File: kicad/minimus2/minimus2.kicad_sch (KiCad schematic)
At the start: 73 parts, among them J1 PROG_SER, J2 LM, J3 LM, Q1 SSM6N58NU_LF, Q2 SSM6N58NU_LF, Q3 DMN3051L, SW1 RESET, SW2 USER_A, SW3 USER_B, U1 LSM6DSRTR, U2 STM32U575CITx, U3 DRV8835, U4 AS5047D, U5 AS5047D, U6 BCR420UFD-7

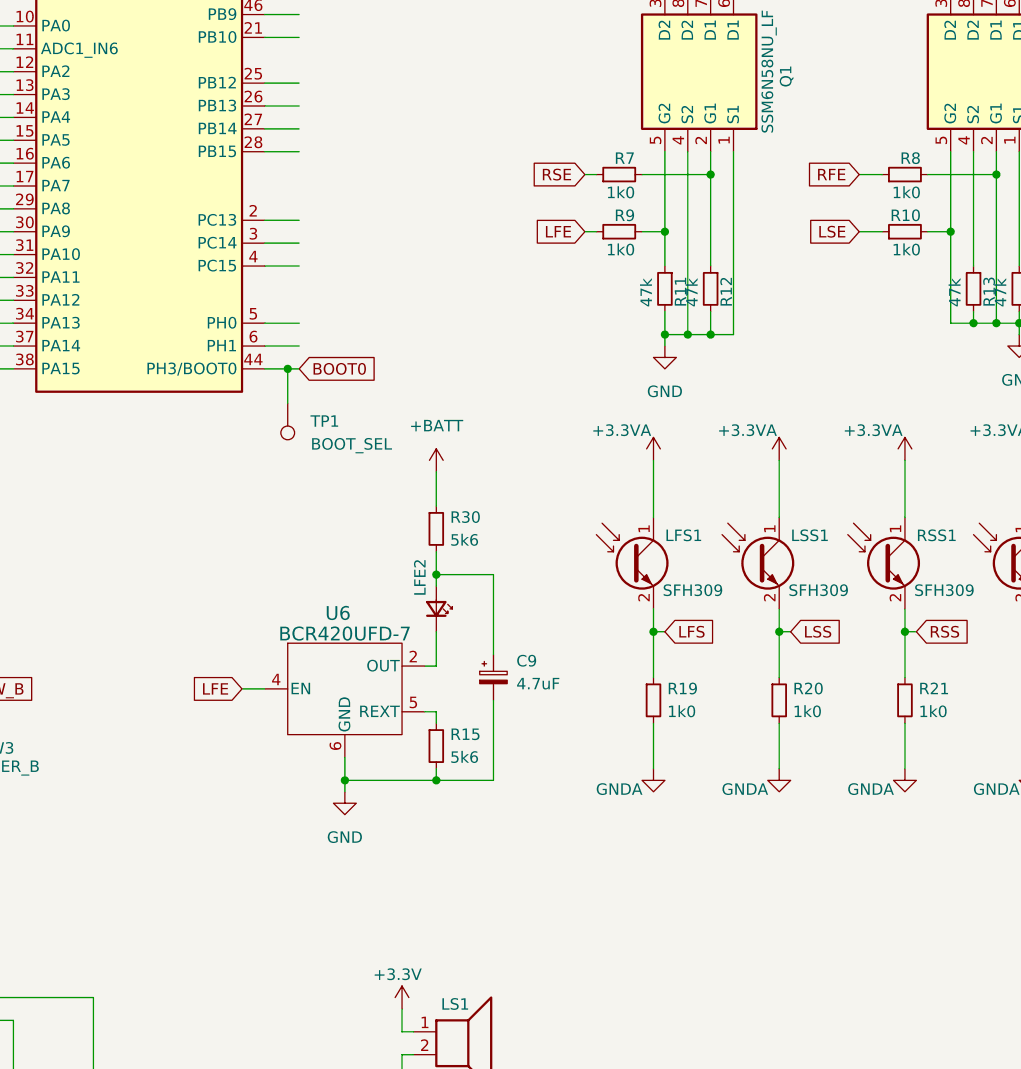
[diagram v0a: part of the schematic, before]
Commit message: rename the sensor emitter nets
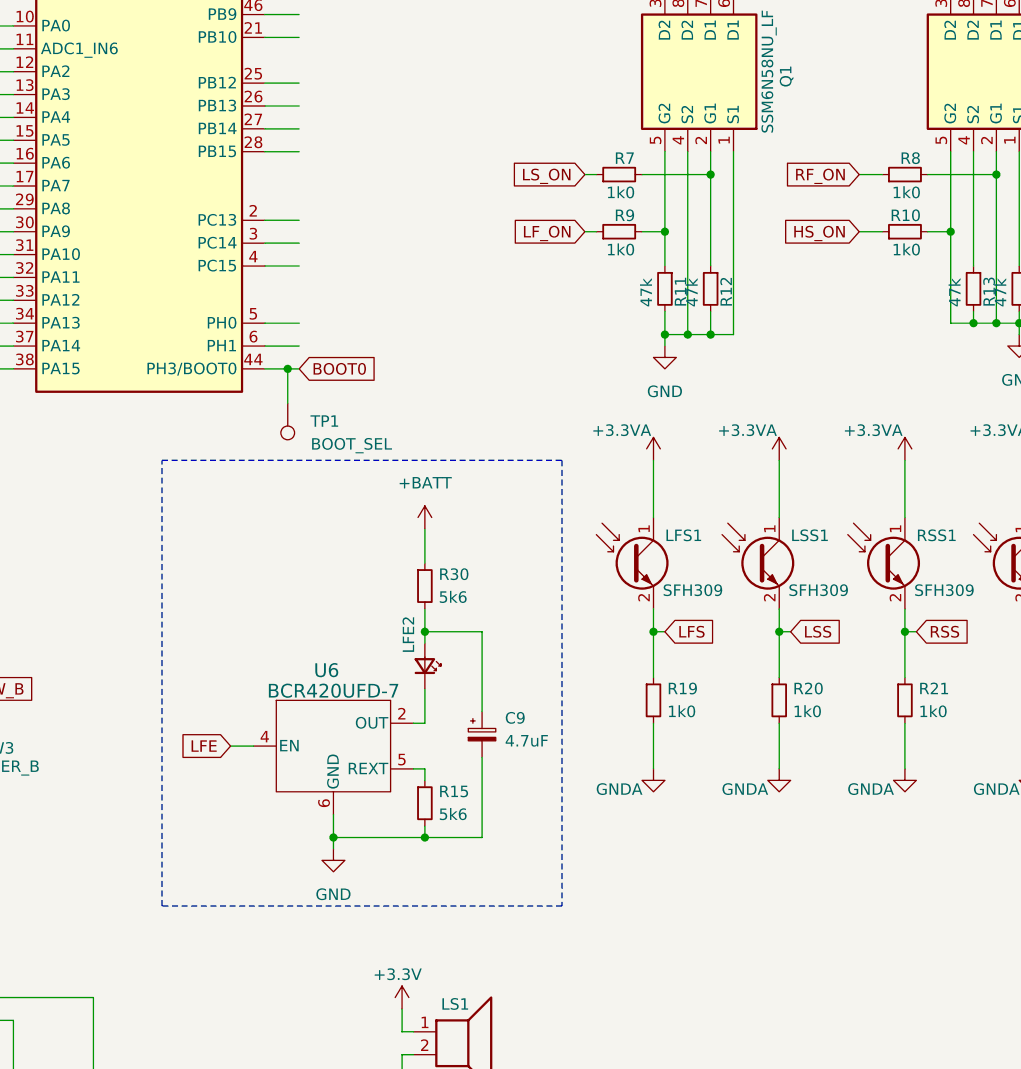
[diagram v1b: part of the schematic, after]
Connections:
- net LFE: no longer R9.1
- net LSE renamed HS_ON
- net RFE renamed RF_ON
- net RSE renamed LS_ON
- new net LF_ON: R9.1
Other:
- moved on the sheet: C9, LFE2, R15, R30, U6

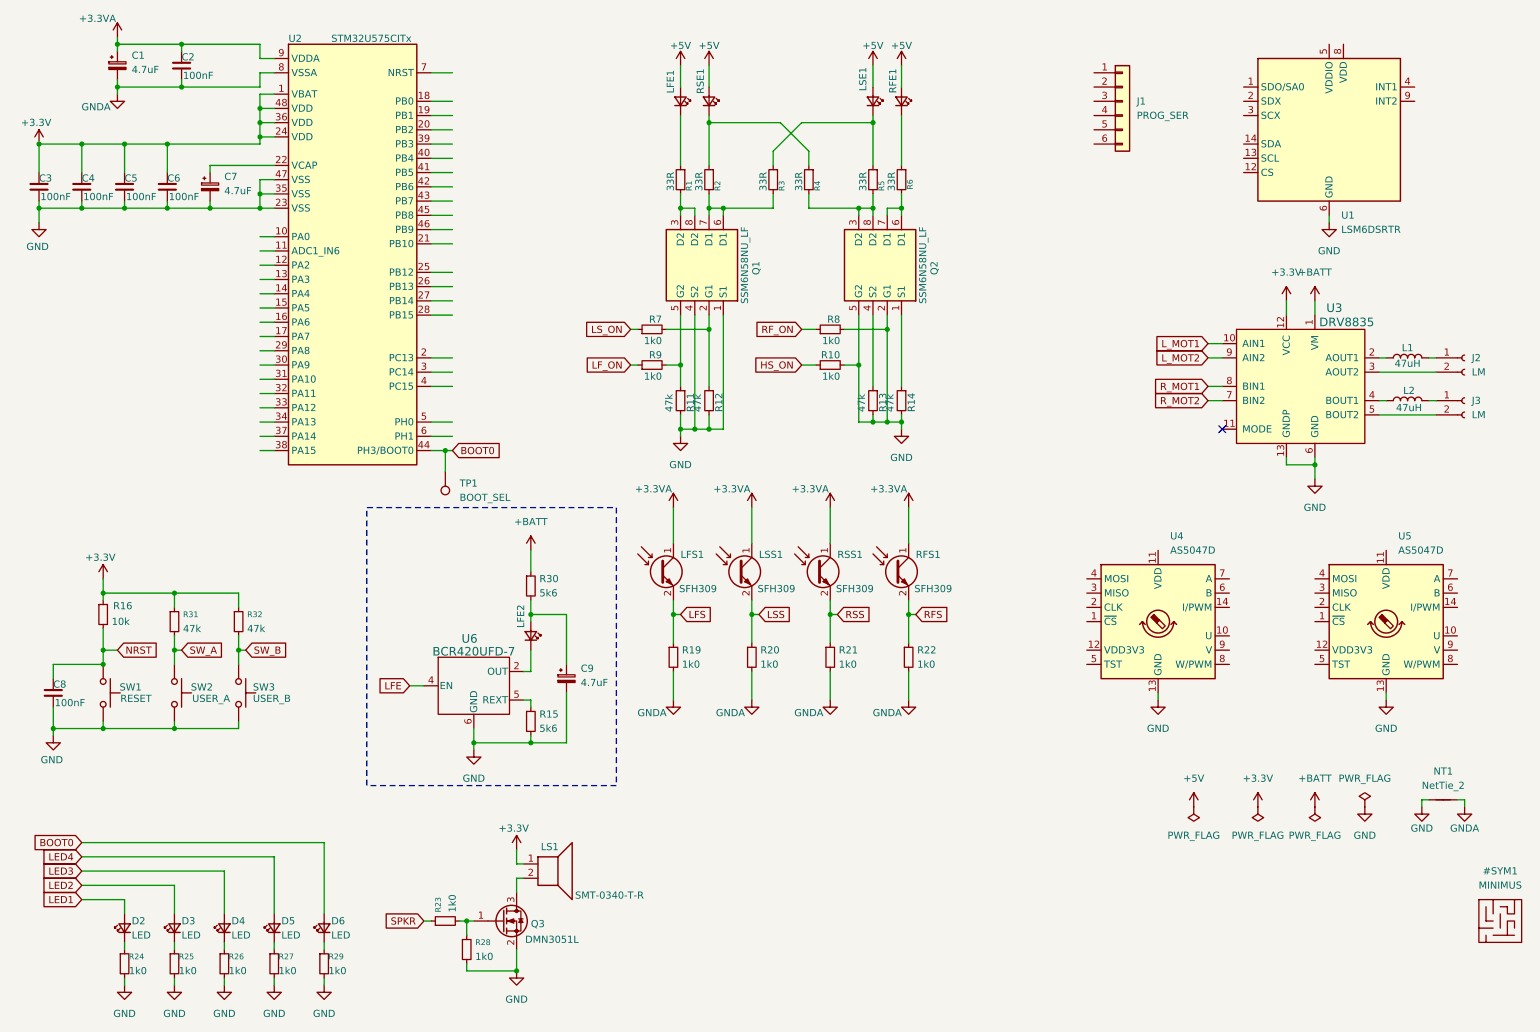
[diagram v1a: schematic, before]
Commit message: remove unused switch and sensor
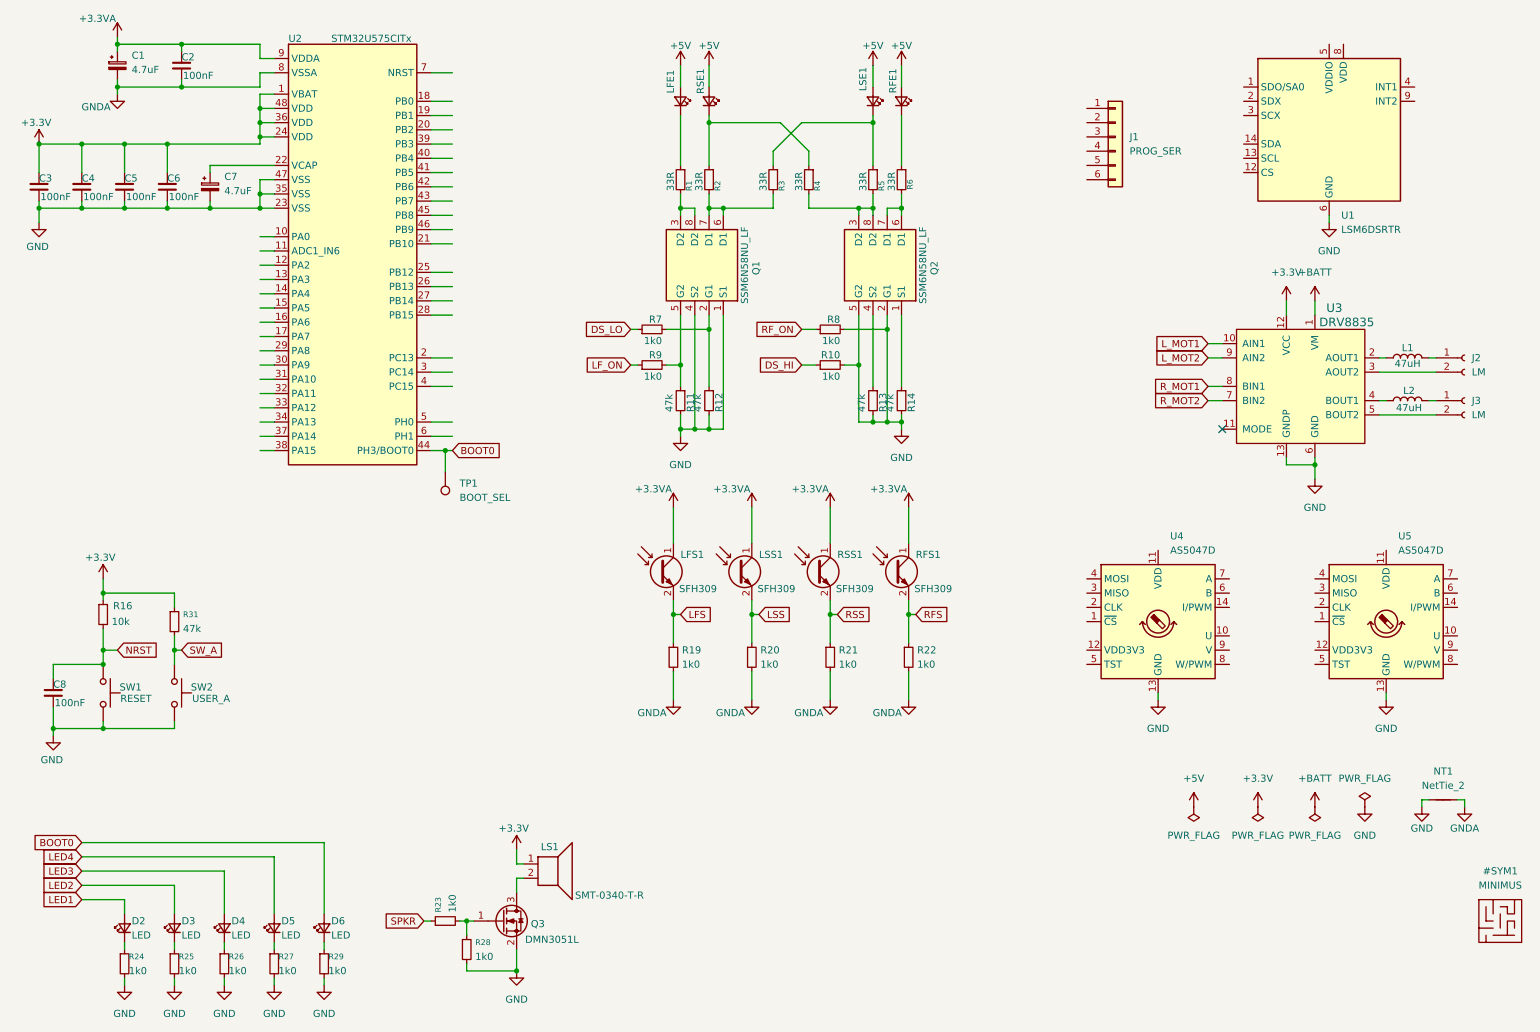
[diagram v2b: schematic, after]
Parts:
- removed C9: 4.7uF, Capacitor_SMD:C_0805_2012Metric, symbol Device:C_Polarized_Small
- removed LFE2: SFH4050, LED_THT:LED_D3.0mm_Horizontal_O1.27mm_Z2.0mm_IRBlack, symbol Device:LED_Small
- removed R15, R30: 5k6, Resistor_SMD:R_0402_1005Metric, symbol Device:R_Small
- removed R32: 47k, Resistor_SMD:R_0402_1005Metric, symbol Device:R_Small
- removed SW3: USER_B, Button_Switch_SMD:SW_Push_1P1T_NO_CK_KMR2, symbol minimus:SW_Push
- removed U6: BCR420UFD-7, U-DFN2020-6_2X2_DIO, symbol BCR420UFD:BCR420UFD-7
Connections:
- net HS_ON renamed DS_HI
- net LS_ON renamed DS_LO
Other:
- moved on the sheet: J1

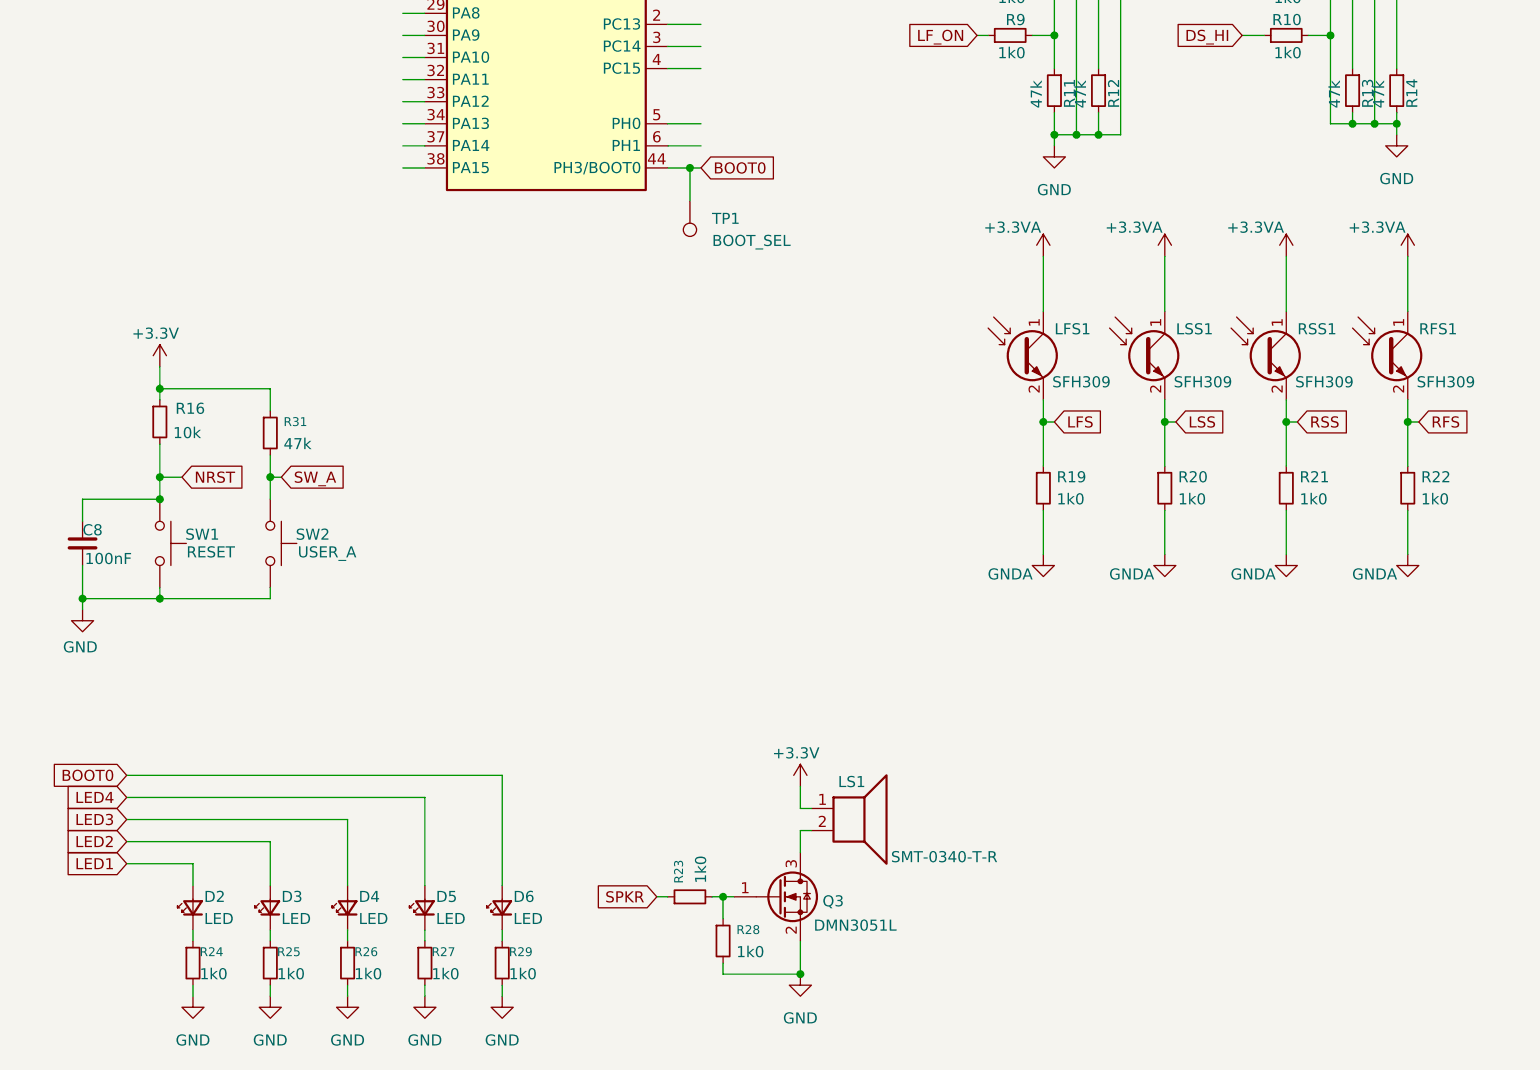
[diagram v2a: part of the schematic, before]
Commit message: add regulators and rotate board
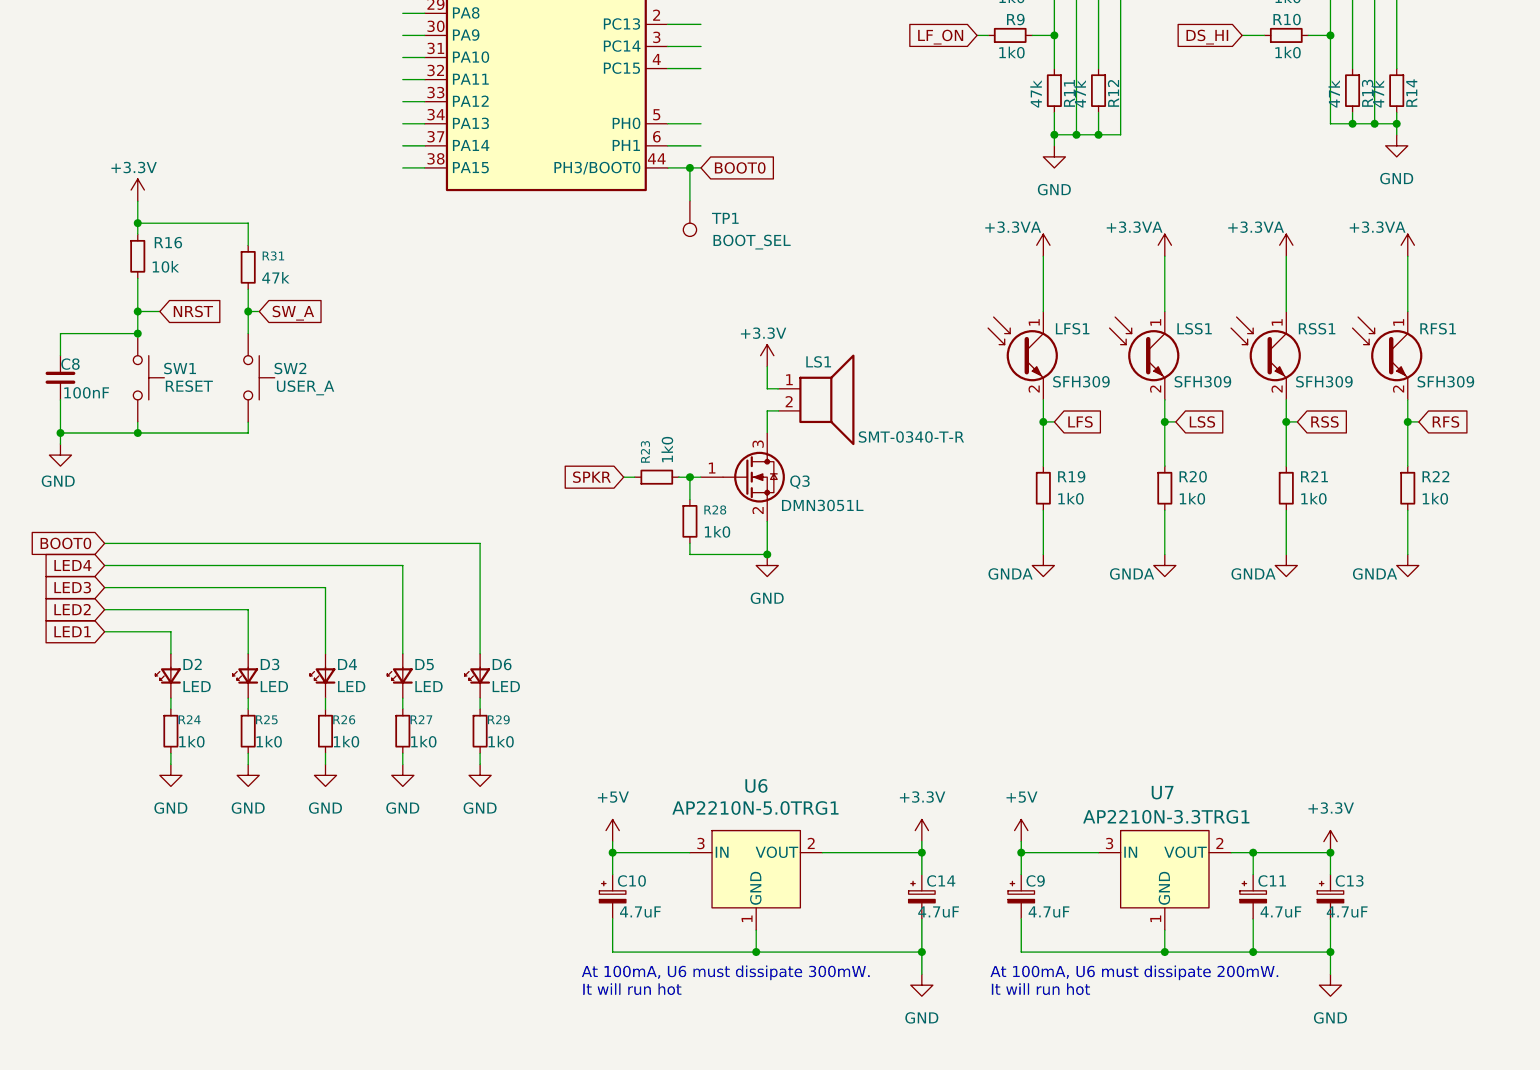
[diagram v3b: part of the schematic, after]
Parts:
- added C10, C11, C13, C14, C9: 4.7uF, Capacitor_SMD:C_0805_2012Metric, symbol Device:C_Polarized_Small
- added U6: AP2210N-5.0TRG1, minimus:AP2210N-x.xTRG1_DIO, symbol minimus:AP2210N-5.0TRG1
- added U7: AP2210N-3.3TRG1, minimus:AP2210N-x.xTRG1_DIO, symbol minimus:AP2210N-3.3TRG1
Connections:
- net +3.3V: now also C11.1, C13.1, C14.1, U6.2 (VOUT), U7.2 (VOUT)
- net +5V: now also C10.1, C9.1, U6.3 (IN), U7.3 (IN)
- net GND: now also C10.2, C11.2, C13.2, C14.2, C9.2, U6.1 (GND), U7.1 (GND)
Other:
- note added: "At 100mA, U6 must dissipate 200mW. It will run hot"
- note added: "At 100mA, U6 must dissipate 300mW. It will run hot"
- moved on the sheet: C8, D2, D3, D4, D5, D6, LS1, Q3, R16, R23, R24, R25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

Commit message: update board footprints
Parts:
- added SW4: SW_SPDT, minimus:CUS-12TB_NDC, symbol Switch:SW_SPDT
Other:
- moved on the sheet: LS1, Q3, R23, R28
